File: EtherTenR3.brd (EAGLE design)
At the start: 68.6 x 53.3 mm, 98 parts, among them IC1 MC33269DT-5.0, IC2 APX811-44UG-7, IC3 ATMEGA16U2-MU, IC4 LM358D, IC5 ATMEGA328P TQFP32, IC6 W5100SQFP80, J1 DC_2_1MM, P1 USB-FT, P2 ICSP:MAIN, P3 ICSP:USB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

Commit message: Beginning of conversion to R3
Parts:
- P1: value USB-FT -> USB-6PSMT; device freetronics-master-v1:USB-MINIB-FT -> freetronics-jon:USB-MICROB-MB05PMXX
- moved C12 5.49 mm to (15.0, 47.1), turned to 270 degrees
- moved C1 3.72 mm to (22.0, 46.5)
- moved P1 3.05 mm to (1.52, 38.1), turned to 270 degrees
- moved SJ1 2.54 mm to (5.95, 42.6)
- moved R1 2.54 mm to (15.0, 43.8)
- moved R2 2.54 mm to (15.0, 40.3)
- moved C2 2.03 mm to (22.0, 43.2)
- moved C8 1.78 mm to (22.0, 39.9)
- moved X1 0.25 mm to (18.5, 43.1)
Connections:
- new net N$3: IC3.28, L3.2, P1.GND, SJ1.1
- net GND: no longer IC3.28, L3.2, P1.GND, SJ1.1
- net N$9: now also P1.FIX1, P1.FIX2, P1.PIN1, P1.PIN2, P1.TAB1, P1.TAB2; no longer P1.SH1, P1.SH2, P1.SH3, P1.SH4
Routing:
- net N$3: track 0.00 -> 18.7 mm, vias 0 -> 2
- net GND: track 210.2 -> 191.7 mm, vias 95 -> 93
- net 5V: track 1223.3 -> 1218.2 mm
- net N$17: track 6.43 -> 9.47 mm
- net N$16: track 6.03 -> 9.00 mm
- net N$9: track 38.7 -> 41.7 mm, vias 0 -> 2
- net D1_TX: track 101.1 -> 103.9 mm
- net N$8: track 5.28 -> 7.82 mm
- net D0_RX: track 105.9 -> 108.2 mm
- net N$113: track 10.5 -> 12.8 mm
- net N$5: track 0.00 -> 1.27 mm
- net MOSI2: track 28.2 -> 27.1 mm
- net SCK2: track 25.5 -> 24.5 mm
- net N$115: track 15.0 -> 14.3 mm, vias 0 -> 4
- net MISO2: track 33.8 -> 33.0 mm
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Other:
- board text added: "SCL"
- board text added: "SDA"

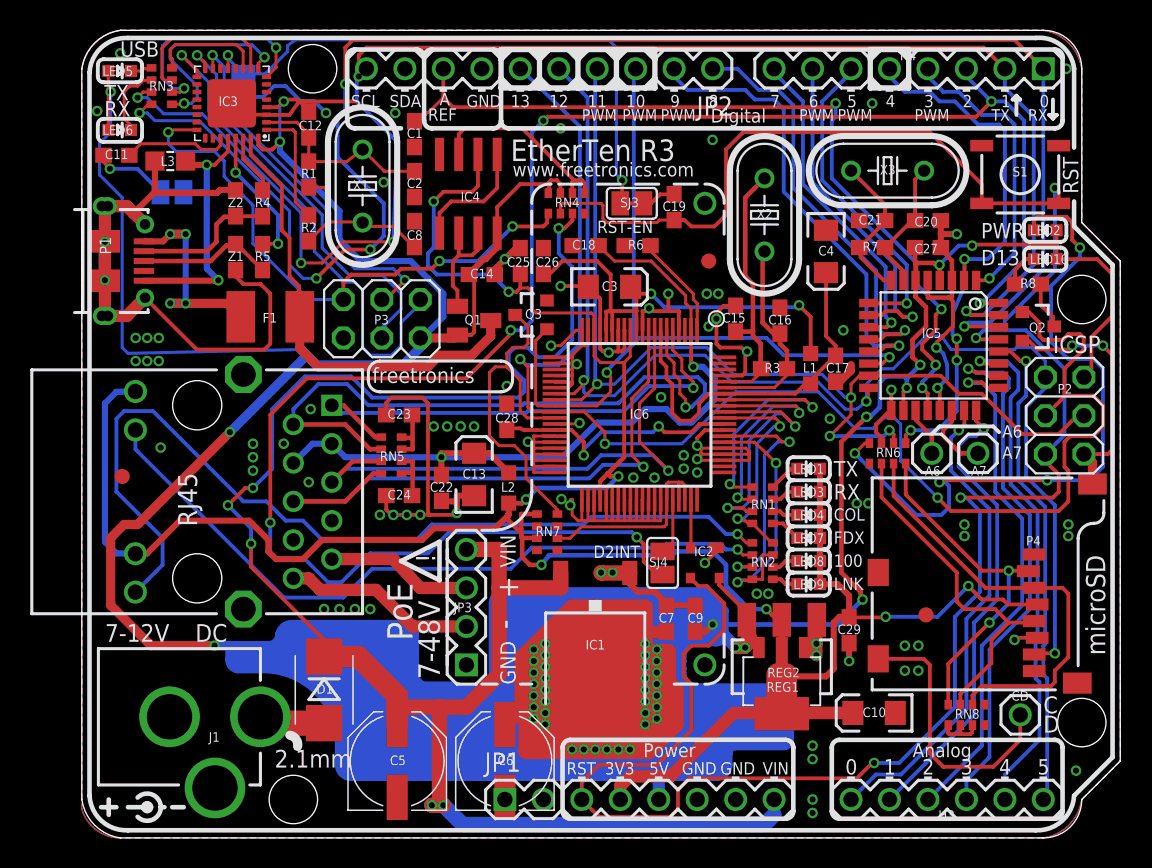
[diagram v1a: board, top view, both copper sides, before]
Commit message: Routing for R3 revision
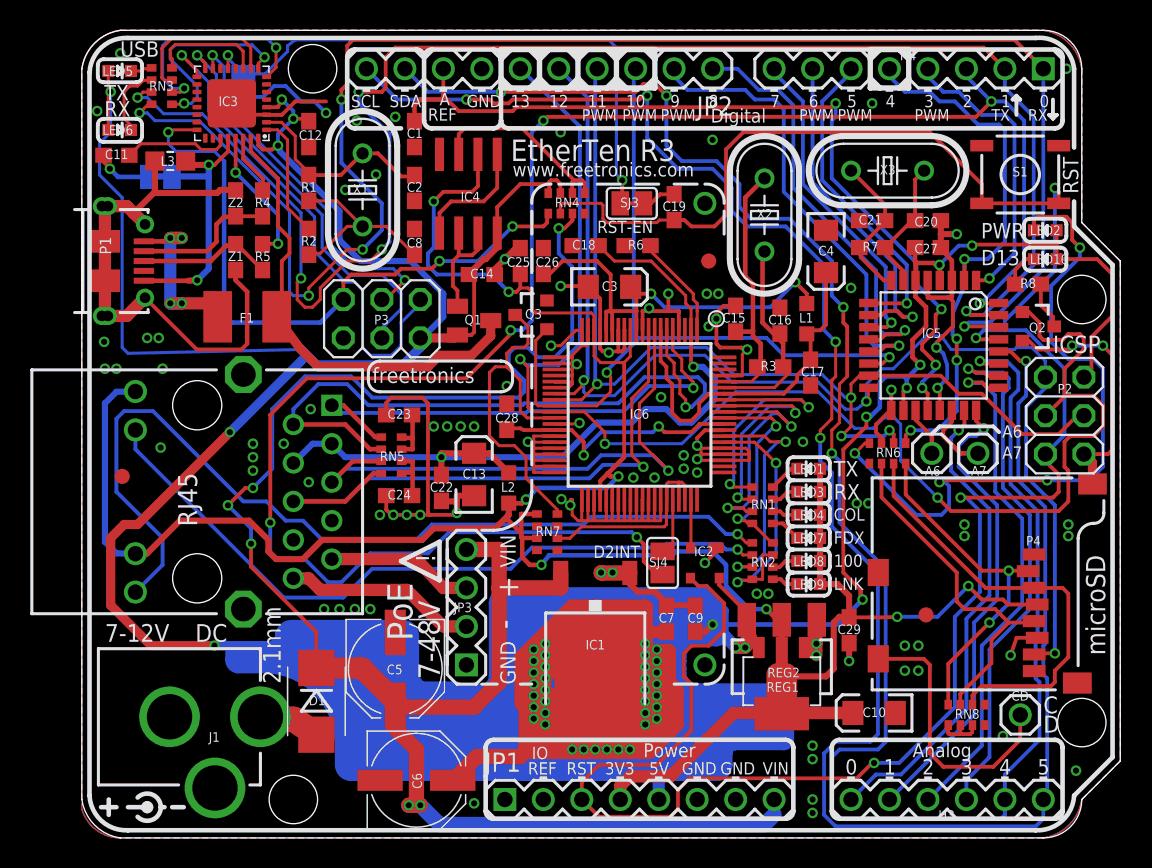
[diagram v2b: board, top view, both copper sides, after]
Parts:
- moved C5 6.10 mm to (20.7, 11.2), turned to 270 degrees
- moved C6 5.98 mm to (22.1, 3.81), turned to 0 degrees
- moved L1 3.31 mm to (47.9, 34.3)
- moved C17 1.67 mm to (48.1, 30.7)
- moved F1 1.52 mm to (10.9, 34.4)
- moved SJ1 1.27 mm to (5.19, 43.7)
- moved D1 0.92 mm to (15.5, 9.02)
- moved R2 0.89 mm to (15.0, 39.4)
- moved R1 0.89 mm to (15.0, 42.9)
- moved C12 0.63 mm to (15.0, 46.5)
- moved C8 0.51 mm to (22.0, 39.4)
- moved R3 0.28 mm to (45.5, 31.1)
- moved C2 0.25 mm to (22.0, 42.9)
- moved X1 0.25 mm to (18.5, 42.8)
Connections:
- removed net A4: IC5.27
- net A4_SDA: now also IC5.27
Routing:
- net A4_SDA: track 0.00 -> 125.5 mm, vias 0 -> 5
- net A5_SCL: track 32.2 -> 128.5 mm, vias 1 -> 5
- net A4: track 32.8 -> 0.00 mm, vias 1 -> 0
- net 5V: track 1218.2 -> 1223.7 mm, vias 50 -> 51
- net RESET2: track 37.5 -> 42.6 mm
- net N$9: track 41.7 -> 36.7 mm, vias 2 -> 0
- net D1_TX: track 103.9 -> 107.7 mm
- net GND: track 191.7 -> 187.9 mm, vias 93 -> 96
- net VIN: track 118.7 -> 120.8 mm
- net N$115: track 14.3 -> 12.3 mm
- net D0_RX: track 108.2 -> 109.9 mm
- net 1V8_OUT: track 30.7 -> 29.3 mm
- net N$114: track 11.5 -> 12.8 mm
- net D11_MOSI: track 70.1 -> 69.1 mm
- net AREF: track 55.5 -> 56.4 mm
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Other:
- board text added: "IO"

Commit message: More routing for R3
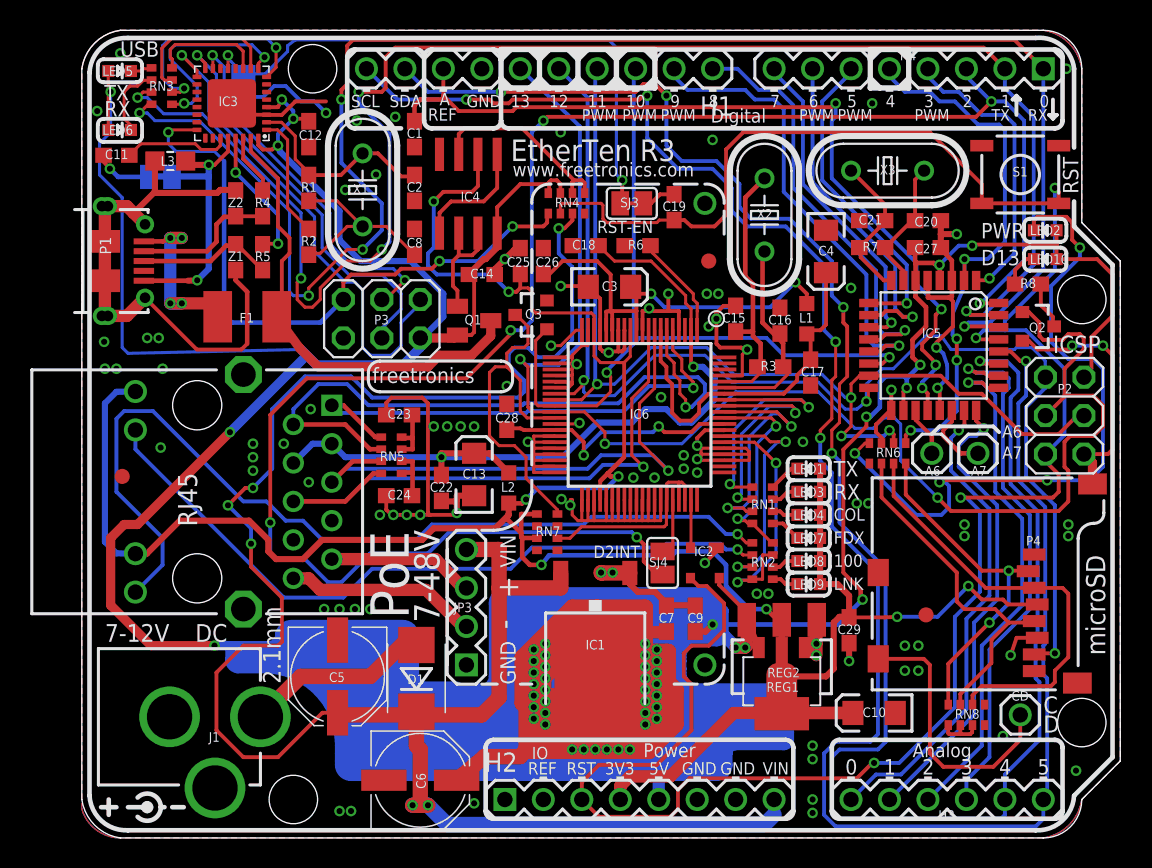
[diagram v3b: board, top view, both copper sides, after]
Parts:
- H1: value M100.1 -> Digital_8_13
- H2: value (none) -> Power
- JP3: value FT-POE-MODULE -> FT-POE-MODULE3; device freetronics-master-v1:FT-POE-MODULE -> freetronics-master-v1.1:FT-POE-MODULE-NOLABEL
- moved D1 6.78 mm to (22.1, 10.5), turned to 90 degrees
- moved C5 3.84 mm to (16.9, 10.7)
- moved C6 0.25 mm to (22.4, 3.81)
- renumbered JP1 to H2, JP2 to H1
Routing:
- net VIN: track 120.8 -> 135.1 mm
- net N$60: track 4.02 -> 12.4 mm
- net GND: vias 96 -> 98
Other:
- board text added: "7-48V"
- board text added: "PoE"

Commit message: Improved I2C and ICSP markings; ERC and DRC for release
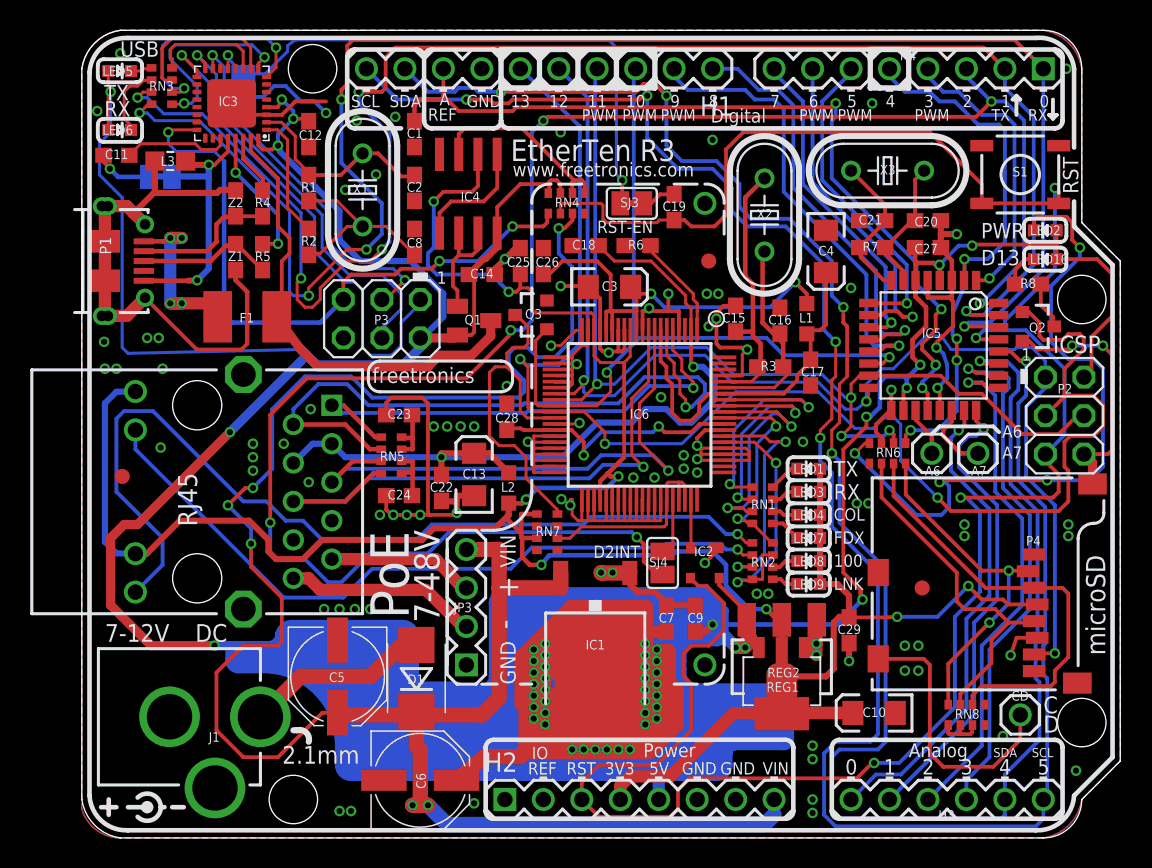
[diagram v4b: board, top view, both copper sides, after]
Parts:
- moved FID2 1.80 mm to (55.5, 16.5)
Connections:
- net N$3 renamed USBGND
- new net N$3: C19.1, SJ3.2
- net DTR: no longer C19.1, SJ3.2
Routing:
- net DTR: track 42.8 -> 39.0 mm
- net N$3: track 0.00 -> 2.28 mm
- net N$5: track 1.27 -> 0.00 mm
- net N$10: track 0.00 -> 1.02 mm
- net N$15: track 0.00 -> 1.02 mm
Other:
- board text added: "I2C"
- board text added: "R3"
- board text added: "v2.0"
- board text removed: "v1.1"
